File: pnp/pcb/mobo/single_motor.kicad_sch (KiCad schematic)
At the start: 8 parts, among them M1 Stepper_Motor

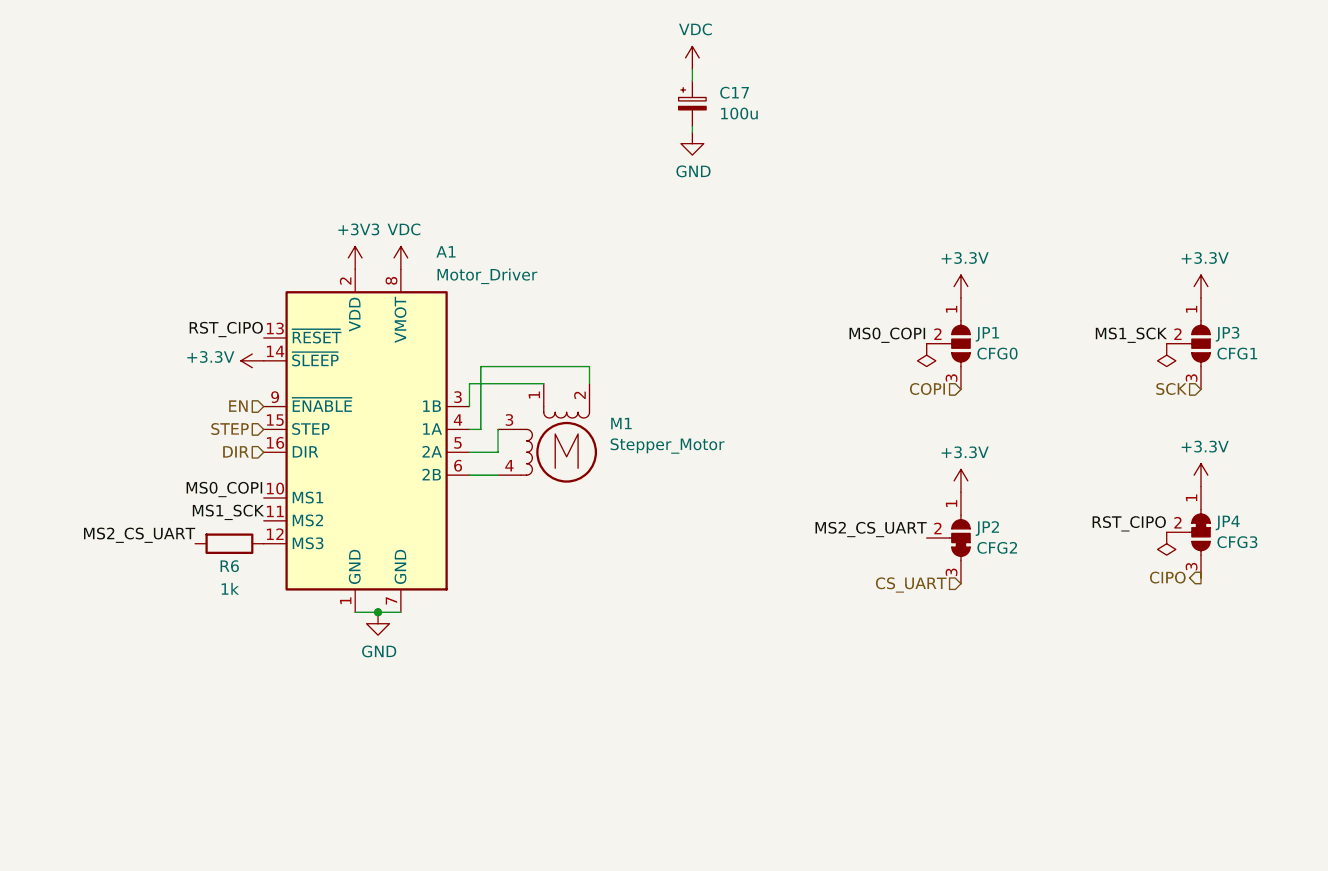
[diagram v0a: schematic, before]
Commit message: Create a hierarchical structure
Put all circuits in to a single-function sheet
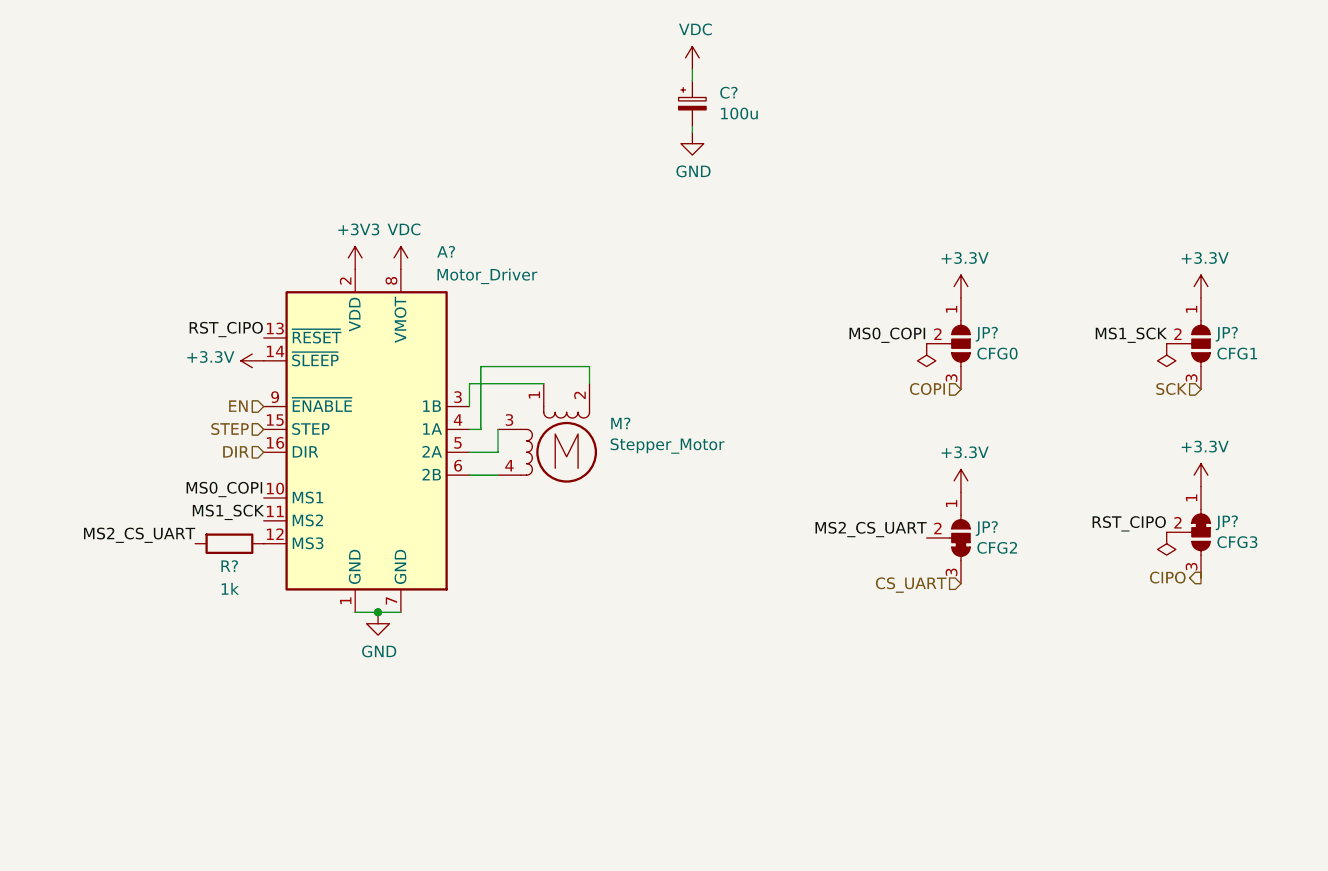
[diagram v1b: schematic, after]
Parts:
- removed A1: Motor_Driver, Module:Pololu_Breakout-16_15.2x20.3mm, symbol Driver_Motor:Pololu_Breakout_A4988
- removed C17: 100u, Capacitor_SMD:CP_Elec_6.3x7.7, symbol Device:C_Polarized_Small
- removed JP1: CFG0, Jumper:SolderJumper-3_P1.3mm_Open_RoundedPad1.0x1.5mm, symbol Jumper:SolderJumper_3_Open
- removed JP2: CFG2, index:SolderJumper-3_P1.3mm_Bridged23_RoundedPad1.0x1.5mm, symbol index:SolderJumper_3_Bridged23
- removed JP3: CFG1, Jumper:SolderJumper-3_P1.3mm_Open_RoundedPad1.0x1.5mm, symbol Jumper:SolderJumper_3_Open
- removed JP4: CFG3, Jumper:SolderJumper-3_P1.3mm_Bridged12_RoundedPad1.0x1.5mm, symbol Jumper:SolderJumper_3_Bridged12
- removed M1: Stepper_Motor, Connector_JST:JST_XH_B4B-XH-A_1x04_P2.50mm_Vertical, symbol Motor:Stepper_Motor_bipolar
- removed R6: 1k, Resistor_SMD:R_0805_2012Metric, symbol Device:R
- added A?: Motor_Driver, Module:Pololu_Breakout-16_15.2x20.3mm, symbol Driver_Motor:Pololu_Breakout_A4988
- added C?: 100u, Capacitor_SMD:CP_Elec_6.3x7.7, symbol Device:C_Polarized_Small
- added JP?: CFG0, Jumper:SolderJumper-3_P1.3mm_Open_RoundedPad1.0x1.5mm, symbol Jumper:SolderJumper_3_Open
- added JP?: CFG2, index:SolderJumper-3_P1.3mm_Bridged23_RoundedPad1.0x1.5mm, symbol index:SolderJumper_3_Bridged23
- added JP?: CFG3, Jumper:SolderJumper-3_P1.3mm_Bridged12_RoundedPad1.0x1.5mm, symbol Jumper:SolderJumper_3_Bridged12
- added JP?: CFG1, Jumper:SolderJumper-3_P1.3mm_Open_RoundedPad1.0x1.5mm, symbol Jumper:SolderJumper_3_Open
- added M?: Stepper_Motor, Connector_JST:JST_XH_B4B-XH-A_1x04_P2.50mm_Vertical, symbol Motor:Stepper_Motor_bipolar
- added R?: 1k, Resistor_SMD:R_0805_2012Metric, symbol Device:R
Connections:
- net +3V3: now also A?.14 (~{SLEEP}), A?.2 (VDD), JP?.1 (A), JP?.1 (A), JP?.1 (A), JP?.1 (B)
- net CIPO: now also JP?.3 (B)
- net COPI: now also JP?.3 (B)
- net CS_UART: now also JP?.3 (A)
- net DIR: now also A?.16 (DIR)
- net EN: now also A?.9 (~{ENABLE})
- net GND: now also A?.1 (GND), A?.7 (GND), C?.2
- net MS0_COPI: now also A?.10 (MS1), JP?.2 (C)
- net MS1_SCK: now also A?.11 (MS2), JP?.2 (C)
- net MS2_CS_UART: now also JP?.2 (C), R?.2
- net RST_CIPO: now also A?.13 (~{RESET}), JP?.2 (C)
- net SCK: now also JP?.3 (B)
- net STEP: now also A?.15 (STEP)
- net VDC: now also A?.8 (VMOT), C?.1
- new net: A?.12 (MS3), R?.1
- new net: A?.3 (1B), M?.1
- new net: A?.4 (1A), M?.2 (-)
- new net: A?.5 (2A), M?.3
- new net: A?.6 (2B), M?.4

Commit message: All sheets cleaned up
All symbols and their fields are now neatly organized.

All hierarchical pins are already imported,
except for the microcontroller sheet.
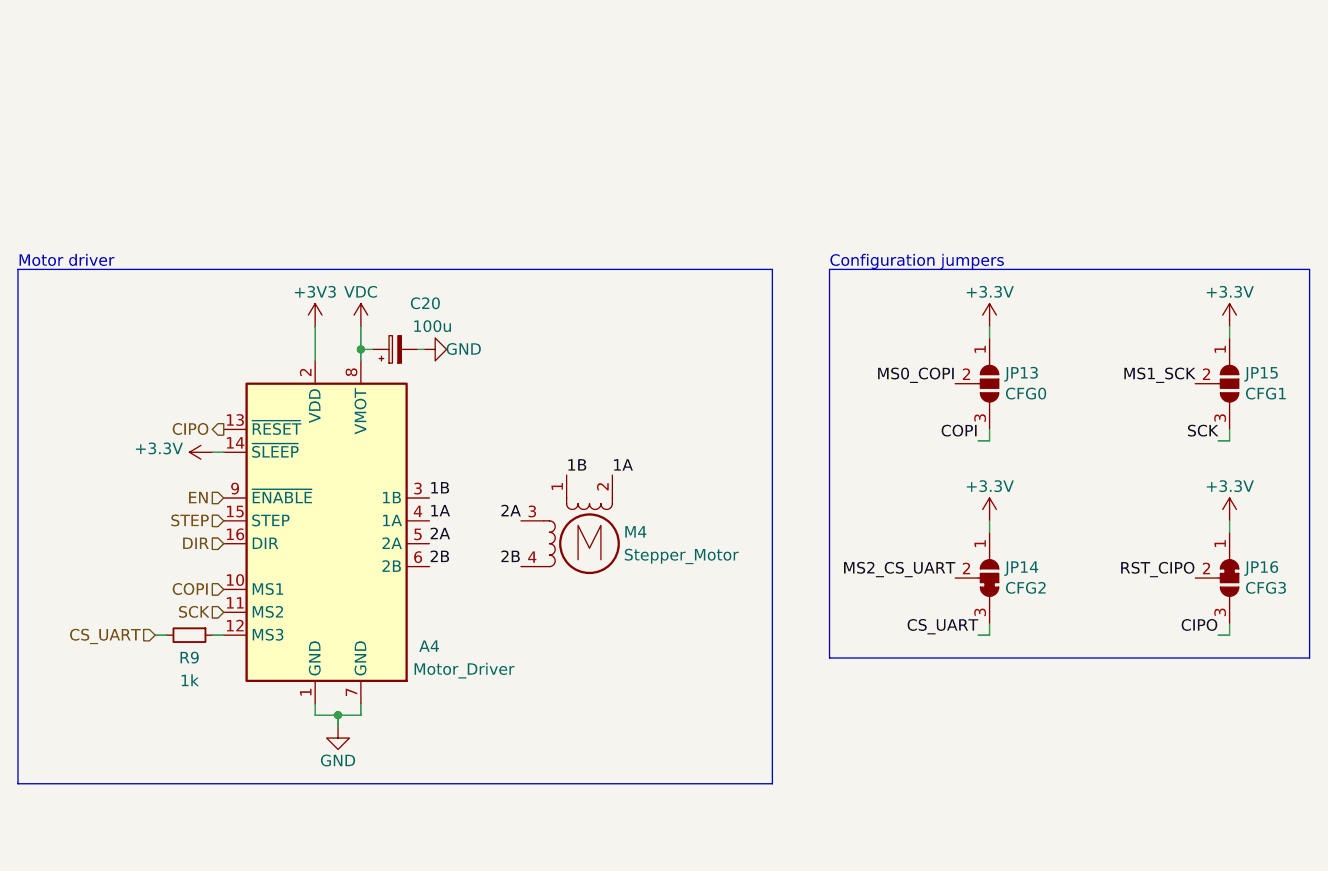
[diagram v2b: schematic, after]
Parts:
- R9: renamed from R?; symbol Device:R -> Device:R_Small
- gave numbers to parts that had none: 7
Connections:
- net CIPO: now also A4.13 (~{RESET})
- net COPI: now also A4.10 (MS1)
- net CS_UART: now also R9.2
- net MS0_COPI: no longer A4.10 (MS1)
- net MS1_SCK: no longer A4.11 (MS2)
- net MS2_CS_UART: no longer R9.2
- net RST_CIPO: no longer A4.13 (~{RESET})
- net SCK: now also A4.11 (MS2)
- net 1B: now reaches A4.3 (1B), M4.1
- net 1A: now reaches A4.4 (1A), M4.2 (-)
- net 2A: now reaches A4.5 (2A), M4.3
- net 2B: now reaches A4.6 (2B), M4.4
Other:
- note added: "Configuration jumpers"
- note added: "Motor driver"
- moved on the sheet: A4, C20, JP13, JP14, JP15, JP16, M4, R9

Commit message: Connect all sub-sheets together
Refactored schematic is checked against existing lay-out.
Connectivity has stayed the same.
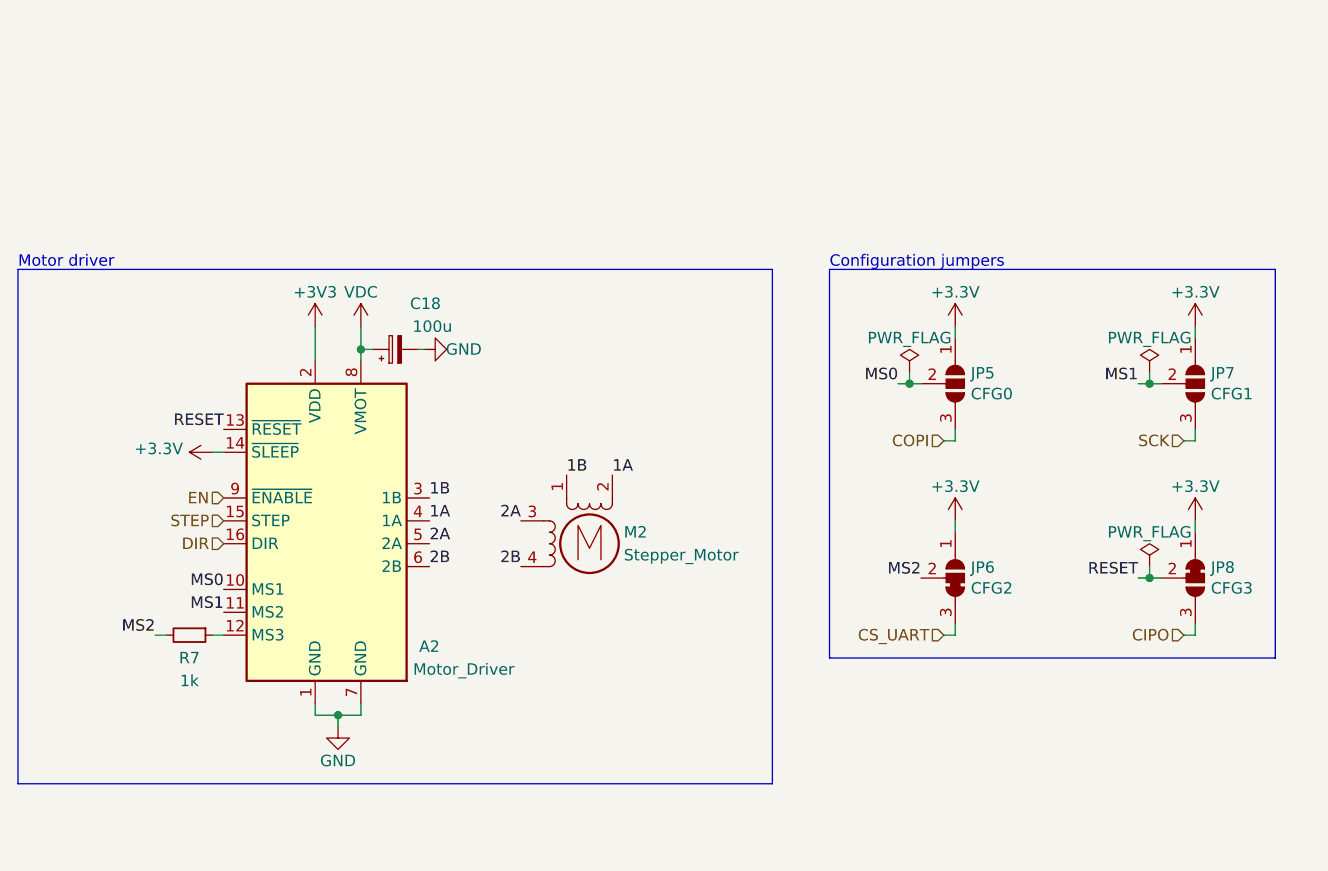
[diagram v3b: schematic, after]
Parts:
- renumbered A4 to A2, C20 to C18, JP13 to JP5, JP14 to JP6, JP15 to JP7, JP16 to JP8, M4 to M2, R9 to R7
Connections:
- net CIPO: no longer A2.13 (~{RESET})
- net COPI: no longer A2.10 (MS1)
- net CS_UART: no longer R7.2
- net SCK: no longer A2.11 (MS2)
- net MS0_COPI renamed MS0
- net MS0: now also A2.10 (MS1)
- net MS1_SCK renamed MS1
- net MS1: now also A2.11 (MS2)
- net MS2_CS_UART renamed MS2
- net MS2: now also R7.2
- net RST_CIPO renamed RESET
- net RESET: now also A2.13 (~{RESET})
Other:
- moved on the sheet: JP5, JP6, JP7, JP8
